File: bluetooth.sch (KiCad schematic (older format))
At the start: 50 parts, among them P100 CONN_2, P110 CONN_1, P111 CONN_1, P112 CONN_1, P113 CONN_1, P114 CONN_1, P115 CONN_1, Q1 MOSFET_N, Q3 MOSFET_N, Q5 MOS_P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

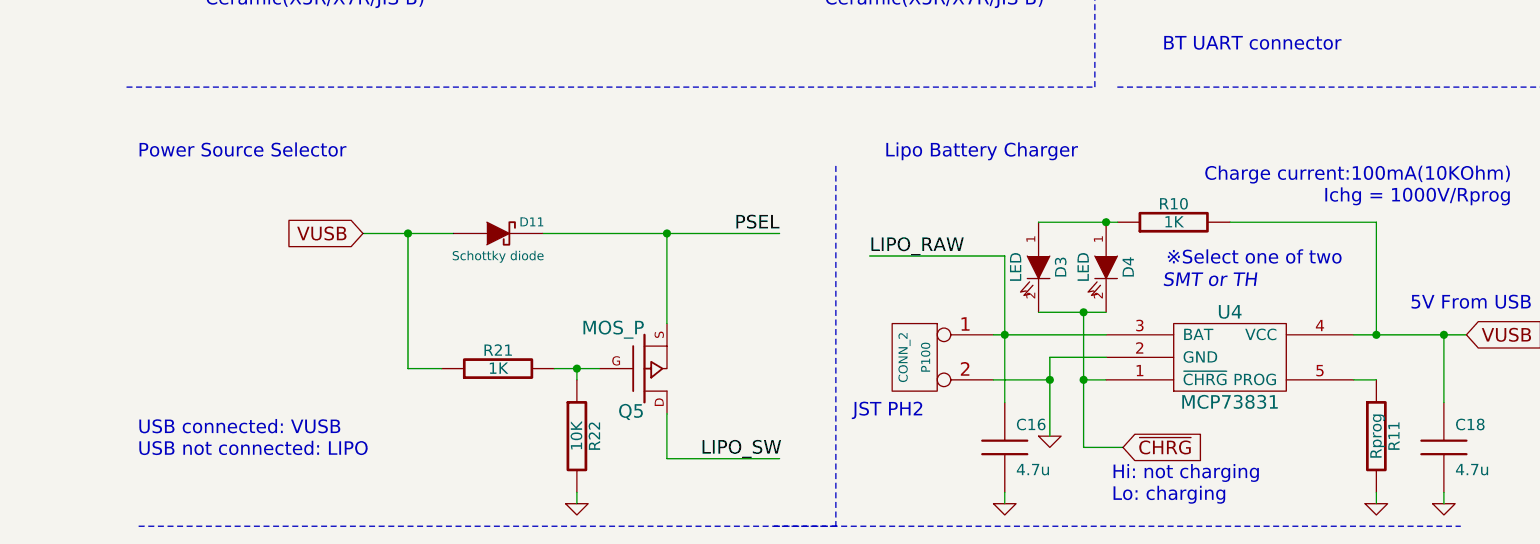
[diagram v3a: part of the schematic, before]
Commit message: Change PTC route to use only for BT
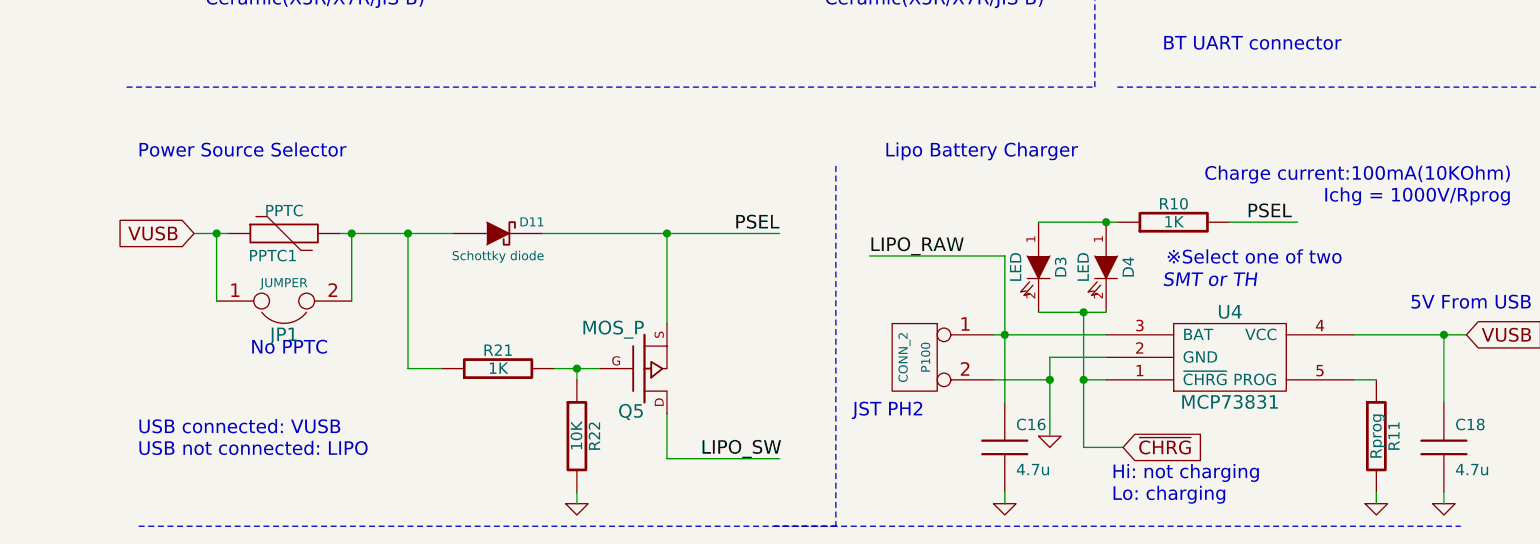
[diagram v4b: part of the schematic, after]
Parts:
- added JP1: JUMPER, symbol JUMPER
- added PPTC1: PPTC, symbol PPTC
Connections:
- wire segments 137 -> 139
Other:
- note added: "No PPTC"
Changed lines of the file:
@@
 JST PH2
 $Comp
-L GND #PWR028
+L GND #PWR027
 U 1 1 51AFD4B7
 P 4750 7150
-F 0 "#PWR028" H 4750 7150 30  0001 C CNN
+F 0 "#PWR027" H 4750 7150 30  0001 C CNN
 F 1 "GND" H 4750 7080 30  0001 C CNN
 F 2 "" H 4750 7150 60  0000 C CNN
@@
 PSEL
 $Comp
-L GND #PWR029
+L GND #PWR028
 U 1 1 51B36189
 P 1600 5150
-F 0 "#PWR029" H 1600 5150 30  0001 C CNN
+F 0 "#PWR028" H 1600 5150 30  0001 C CNN
 F 1 "GND" H 1600 5080 30  0001 C CNN
 F 2 "" H 1600 5150 60  0000 C CNN
@@
 $EndComp
 $Comp
-L GND #PWR030
+L GND #PWR029
 U 1 1 51B36198
 P 4350 5150
-F 0 "#PWR030" H 4350 5150 30  0001 C CNN
+F 0 "#PWR029" H 4350 5150 30  0001 C CNN
 F 1 "GND" H 4350 5080 30  0001 C CNN
 F 2 "" H 4350 5150 60  0000 C CNN
@@
 $EndComp
 $Comp
-L GND #PWR031
+L GND #PWR030
 U 1 1 51B36208
 P 3400 5150
-F 0 "#PWR031" H 3400 5150 30  0001 C CNN
+F 0 "#PWR030" H 3400 5150 30  0001 C CNN
 F 1 "GND" H 3400 5080 30  0001 C CNN
 F 2 "" H 3400 5150 60  0000 C CNN
@@
 $EndComp
 $Comp
-L GND #PWR032
+L GND #PWR031
 U 1 1 51B4212D
 P 1250 3150
-F 0 "#PWR032" H 1250 3150 30  0001 C CNN
+F 0 "#PWR031" H 1250 3150 30  0001 C CNN
 F 1 "GND" H 1250 3080 30  0001 C CNN
 F 2 "" H 1250 3150 60  0000 C CNN
@@
 $EndComp
 $Comp
-L GND #PWR033
+L GND #PWR032
 U 1 1 51B4213C
 P 3300 3150
-F 0 "#PWR033" H 3300 3150 30  0001 C CNN
+F 0 "#PWR032" H 3300 3150 30  0001 C CNN
 F 1 "GND" H 3300 3080 30  0001 C CNN
 F 2 "" H 3300 3150 60  0000 C CNN
@@
 $EndComp
 $Comp
-L GND #PWR034
+L GND #PWR033
 U 1 1 51B421C0
 P 1650 3150
-F 0 "#PWR034" H 1650 3150 30  0001 C CNN
+F 0 "#PWR033" H 1650 3150 30  0001 C CNN
 F 1 "GND" H 1650 3080 30  0001 C CNN
 F 2 "" H 1650 3150 60  0000 C CNN
@@
 $EndComp
 $Comp
-L GND #PWR035
+L GND #PWR034
 U 1 1 51B42259
 P 3000 3350
-F 0 "#PWR035" H 3000 3350 30  0001 C CNN
+F 0 "#PWR034" H 3000 3350 30  0001 C CNN
 F 1 "GND" H 3000 3280 30  0001 C CNN
 F 2 "" H 3000 3350 60  0000 C CNN
@@
 $EndComp
 $Comp
-L GND #PWR036
+L GND #PWR035
 U 1 1 51B4294A
 P 4650 2050
-F 0 "#PWR036" H 4650 2050 30  0001 C CNN
+F 0 "#PWR035" H 4650 2050 30  0001 C CNN
 F 1 "GND" H 4650 1980 30  0001 C CNN
 F 2 "" H 4650 2050 60  0000 C CNN
@@
 $EndComp
 $Comp
-L +5V #PWR037
+L +5V #PWR036
 U 1 1 51B42AA7
 P 1850 1025
-F 0 "#PWR037" H 1850 1115 20  0001 C CNN
+F 0 "#PWR036" H 1850 1115 20  0001 C CNN
 F 1 "+5V" H 1850 1115 30  0000 C CNN
 F 2 "" H 1850 1025 60  0000 C CNN
@@
 $EndComp
 $Comp
-L +3.3V #PWR038
+L +3.3V #PWR037
 U 1 1 51B42AB6
 P 950 1025
-F 0 "#PWR038" H 950 985 30  0001 C CNN
+F 0 "#PWR037" H 950 985 30  0001 C CNN
 F 1 "+3.3V" H 950 1135 30  0000 C CNN
 F 2 "" H 950 1025 60  0000 C CNN
@@
 $EndComp
 $Comp
-L GND #PWR039
+L GND #PWR038
 U 1 1 51B44001
 P 6200 7450
-F 0 "#PWR039" H 6200 7450 30  0001 C CNN
+F 0 "#PWR038" H 6200 7450 30  0001 C CNN
 F 1 "GND" H 6200 7380 30  0001 C CNN
 F 2 "" H 6200 7450 60  0000 C CNN
@@
 BT UART connector
 $Comp
-L +3.3V #PWR040
+L +3.3V #PWR039
 U 1 1 51B8A63B
 P 6100 4350
-F 0 "#PWR040" H 6100 4310 30  0001 C CNN
+F 0 "#PWR039" H 6100 4310 30  0001 C CNN
 F 1 "+3.3V" H 6100 4460 30  0000 C CNN
 F 2 "" H 6100 4350 60  0000 C CNN
@@
 $EndComp
 $Comp
-L GND #PWR041
+L GND #PWR040
 U 1 1 51B8A64A
 P 6100 4950
-F 0 "#PWR041" H 6100 4950 30  0001 C CNN
+F 0 "#PWR040" H 6100 4950 30  0001 C CNN
 F 1 "GND" H 6100 4880 30  0001 C CNN
 F 2 "" H 6100 4950 60  0000 C CNN
@@
 $EndComp
 $Comp
-L GND #PWR042
+L GND #PWR041
 U 1 1 51B8BF6B
 P 6500 7450
-F 0 "#PWR042" H 6500 7450 30  0001 C CNN
+F 0 "#PWR041" H 6500 7450 30  0001 C CNN
 F 1 "GND" H 6500 7380 30  0001 C CNN
 F 2 "" H 6500 7450 60  0000 C CNN
@@
 $EndComp
 $Comp
-L GND #PWR043
+L GND #PWR042
 U 1 1 51BE968F
 P 8550 6950
-F 0 "#PWR043" H 8550 6950 30  0001 C CNN
+F 0 "#PWR042" H 8550 6950 30  0001 C CNN
 F 1 "GND" H 8550 6880 30  0001 C CNN
 F 2 "" H 8550 6950 60  0000 C CNN
@@
 $EndComp
 $Comp
-L GND #PWR044
+L GND #PWR043
 U 1 1 52B7B3EE
 P 9875 3325
-F 0 "#PWR044" H 9875 3325 30  0001 C CNN
+F 0 "#PWR043" H 9875 3325 30  0001 C CNN
 F 1 "GND" H 9875 3255 30  0001 C CNN
 F 2 "" H 9875 3325 60  0000 C CNN
@@
 FACTORY_RESET
 $Comp
-L +3.3V #PWR045
+L +3.3V #PWR044
 U 1 1 52B7F387
 P 7600 750
-F 0 "#PWR045" H 7600 710 30  0001 C CNN
+F 0 "#PWR044" H 7600 710 30  0001 C CNN
 F 1 "+3.3V" H 7600 860 30  0000 C CNN
 F 2 "" H 7600 750 60  0000 C CNN
@@
 F.RST is not implemented,\nbe shorted with tweezer.\nON-OFF-ON-OFF-ON\nto restore factory default.\nPower on with turning ON.
 $Comp
-L +3.3V #PWR046
+L +3.3V #PWR045
 U 1 1 52B7F708
 P 7575 2850
-F 0 "#PWR046" H 7575 2810 30  0001 C CNN
+F 0 "#PWR045" H 7575 2810 30  0001 C CNN
 F 1 "+3.3V" H 7575 2960 30  0000 C CNN
 F 2 "" H 7575 2850 60  0000 C CNN
@@
 $EndComp
 $Comp
-L +5V #PWR047
+L +5V #PWR046
 U 1 1 52B840DE
 P 3775 1025
-F 0 "#PWR047" H 3775 1115 20  0001 C CNN
+F 0 "#PWR046" H 3775 1115 20  0001 C CNN
 F 1 "+5V" H 3775 1115 30  0000 C CNN
 F 2 "" H 3775 1025 60  0000 C CNN
@@
 $EndComp
 $Comp
-L +3.3V #PWR048
+L +3.3V #PWR047
 U 1 1 52B840E4
 P 2875 1025
-F 0 "#PWR048" H 2875 985 30  0001 C CNN
+F 0 "#PWR047" H 2875 985 30  0001 C CNN
 F 1 "+3.3V" H 2875 1135 30  0000 C CNN
 F 2 "" H 2875 1025 60  0000 C CNN
@@
 Text Notes 700  5925 0    60   ~ 0
 Power Source Selector
-Text GLabel 1700 6250 0    60   Input ~ 0
+Text GLabel 950  6250 0    60   Input ~ 0
 VUSB
 $Comp
@@
 PSEL
 $Comp
-L GND #PWR049
+L GND #PWR048
 U 1 1 5310D0A7
 P 2650 7450
-F 0 "#PWR049" H 2650 7450 30  0001 C CNN
+F 0 "#PWR048" H 2650 7450 30  0001 C CNN
 F 1 "GND" H 2650 7380 30  0001 C CNN
 F 2 "" H 2650 7450 60  0000 C CNN
@@
 $EndComp
 $Comp
-L +5V #PWR050
+L +5V #PWR049
 U 1 1 5310EAB1
 P 1400 4300
-F 0 "#PWR050" H 1400 4390 20  0001 C CNN
+F 0 "#PWR049" H 1400 4390 20  0001 C CNN
 F 1 "+5V" H 1400 4390 30  0000 C CNN
 F 2 "" H 1400 4300 60  0000 C CNN
@@
 $EndComp
 $Comp
-L +5V #PWR051
+L +5V #PWR050
 U 1 1 5310EB6D
 P 950 2550
-F 0 "#PWR051" H 950 2640 20  0001 C CNN
+F 0 "#PWR050" H 950 2640 20  0001 C CNN
 F 1 "+5V" H 950 2640 30  0000 C CNN
 F 2 "" H 950 2550 60  0000 C CNN
@@
 LIPO_RAW
 $Comp
-L +3.3V #PWR052
+L +3.3V #PWR051
 U 1 1 5315633E
 P 10950 4700
-F 0 "#PWR052" H 10950 4660 30  0001 C CNN
+F 0 "#PWR051" H 10950 4660 30  0001 C CNN
 F 1 "+3.3V" H 10950 4810 30  0000 C CNN
 F 2 "" H 10950 4700 60  0000 C CNN
@@
 LIPO_RAW
 $Comp
-L +3.3V #PWR053
+L +3.3V #PWR052
 U 1 1 5316AB09
 P 8325 2225
-F 0 "#PWR053" H 8325 2185 30  0001 C CNN
+F 0 "#PWR052" H 8325 2185 30  0001 C CNN
 F 1 "+3.3V" H 8325 2335 30  0000 C CNN
 F 2 "" H 8325 2225 60  0000 C CNN
@@
 $EndComp
 $Comp
-L GND #PWR054
+L GND #PWR053
 U 1 1 53177DE3
 P 5250 2050
-F 0 "#PWR054" H 5250 2050 30  0001 C CNN
+F 0 "#PWR053" H 5250 2050 30  0001 C CNN
 F 1 "GND" H 5250 1980 30  0001 C CNN
 F 2 "" H 5250 2050 60  0000 C CNN
@@
 $EndComp
 $Comp
-L +5V #PWR055
+L +5V #PWR054
 U 1 1 531B3A32
 P 10100 5750
-F 0 "#PWR055" H 10100 5840 20  0001 C CNN
+F 0 "#PWR054" H 10100 5840 20  0001 C CNN
 F 1 "+5V" H 10100 5840 30  0000 C CNN
 F 2 "" H 10100 5750 60  0000 C CNN
@@
 $EndComp
 $Comp
-L GND #PWR056
+L GND #PWR055
 U 1 1 53B572EF
 P 4550 7450
-F 0 "#PWR056" H 4550 7450 30  0001 C CNN
+F 0 "#PWR055" H 4550 7450 30  0001 C CNN
 F 1 "GND" H 4550 7380 30  0001 C CNN
 F 2 "" H 4550 7450 60  0000 C CNN
@@
 $EndComp
 $Comp
-L GND #PWR057
+L GND #PWR056
 U 1 1 53C70129
 P 5900 2050
-F 0 "#PWR057" H 5900 2050 30  0001 C CNN
+F 0 "#PWR056" H 5900 2050 30  0001 C CNN
 F 1 "GND" H 5900 1980 30  0001 C CNN
 F 2 "" H 5900 2050 60  0000 C CNN
@@
 	4900 6900 5000 6900
 Wire Wire Line
-	5550 6200 6200 6200
-Wire Wire Line
-	6200 6200 6200 6700
-Connection ~ 6200 6700
-Wire Wire Line
 	6100 6900 6200 6900
 Wire Wire Line
@@
 	3325 1175 2875 1175
 Wire Wire Line
-	1700 6250 2100 6250
+	1600 6250 2100 6250
 Wire Wire Line
 	1900 6250 1900 6850
@@
 	10950 4700 10950 4825
 $Comp
-L PWR_FLAG #FLG058
+L PWR_FLAG #FLG057
 U 1 1 531F4430
 P 10950 4825
-F 0 "#FLG058" H 10950 4920 30  0001 C CNN
+F 0 "#FLG057" H 10950 4920 30  0001 C CNN
 F 1 "PWR_FLAG" H 10950 5005 30  0000 C CNN
 F 2 "" H 10950 4825 60  0000 C CNN
@@
 $EndComp
 Connection ~ 10950 4775
+Wire Wire Line
+	1650 6550 1650 6250
+Wire Wire Line
+	1050 6550 1050 6250
+Text Notes 1200 6800 0    60   ~ 0
+No PPTC
+$Comp
+L PPTC PPTC1
+U 1 1 540C4258
+P 1350 6250
+F 0 "PPTC1" H 1300 6350 50  0000 C CNN
+F 1 "PPTC" H 1350 6150 50  0000 C CNN
+F 2 "" V 1350 6250 60  0000 C CNN
+F 3 "" V 1350 6250 60  0000 C CNN
+	1    1350 6250
+	1    0    0    1
+$EndComp
+$Comp
+L JUMPER JP1
+U 1 1 540C425F
+P 1350 6550
+F 0 "JP1" H 1350 6700 60  0000 C CNN
+F 1 "JUMPER" H 1350 6470 40  0000 C CNN
+F 2 "" H 1350 6550 60  0000 C CNN
+F 3 "" H 1350 6550 60  0000 C CNN
+	1    1350 6550
+	1    0    0    1
+$EndComp
+Wire Wire Line
+	1100 6250 950  6250
+Connection ~ 1650 6250
+Connection ~ 1050 6250
+Text Label 5625 6200 0    60   ~ 0
+PSEL
+Wire Wire Line
+	5550 6200 5850 6200
 $EndSCHEMATC
